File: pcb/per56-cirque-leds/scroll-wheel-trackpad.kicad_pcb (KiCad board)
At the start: 2 copper layers, 64.8 x 63.5 mm, 13 parts, among them J2 Conn_01x12_Female, SW1 RotaryEncoder

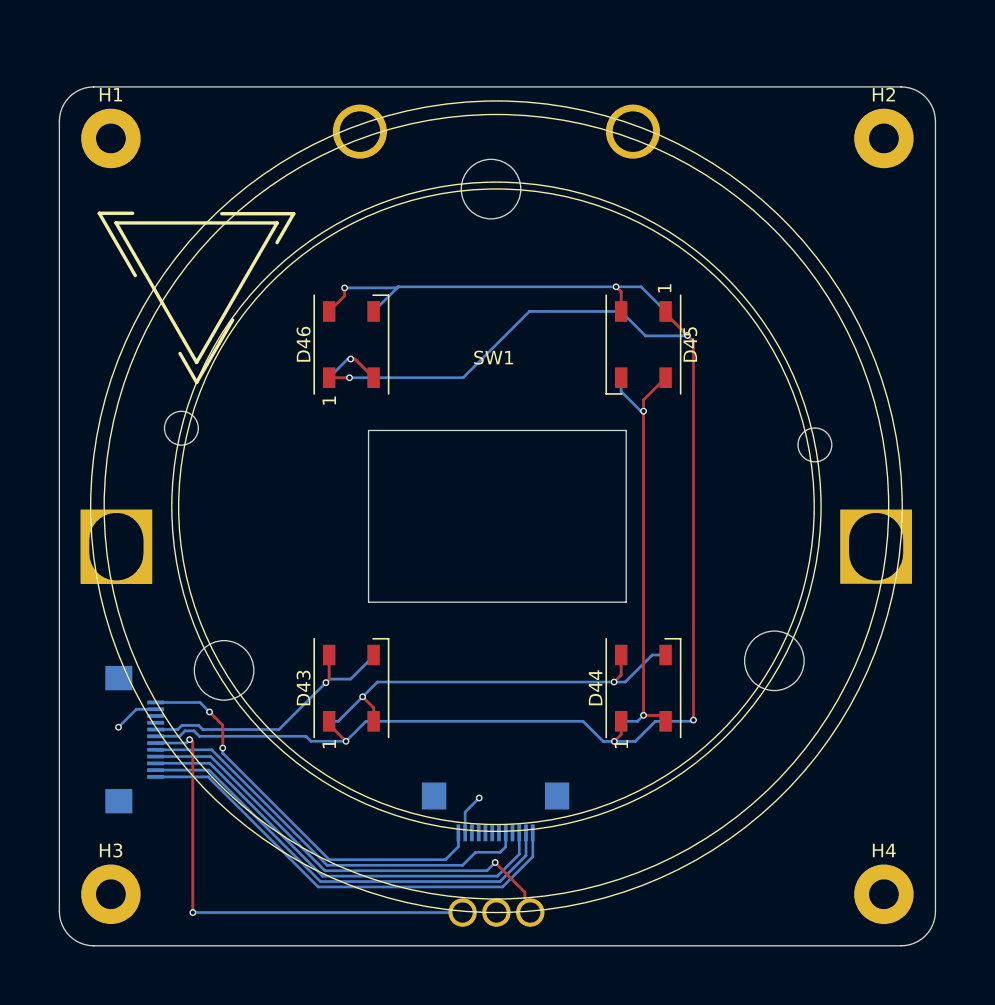
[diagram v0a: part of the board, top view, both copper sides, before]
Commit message: updated a few things, including standard pcb sizes and mounting, 3v3 logic level specification
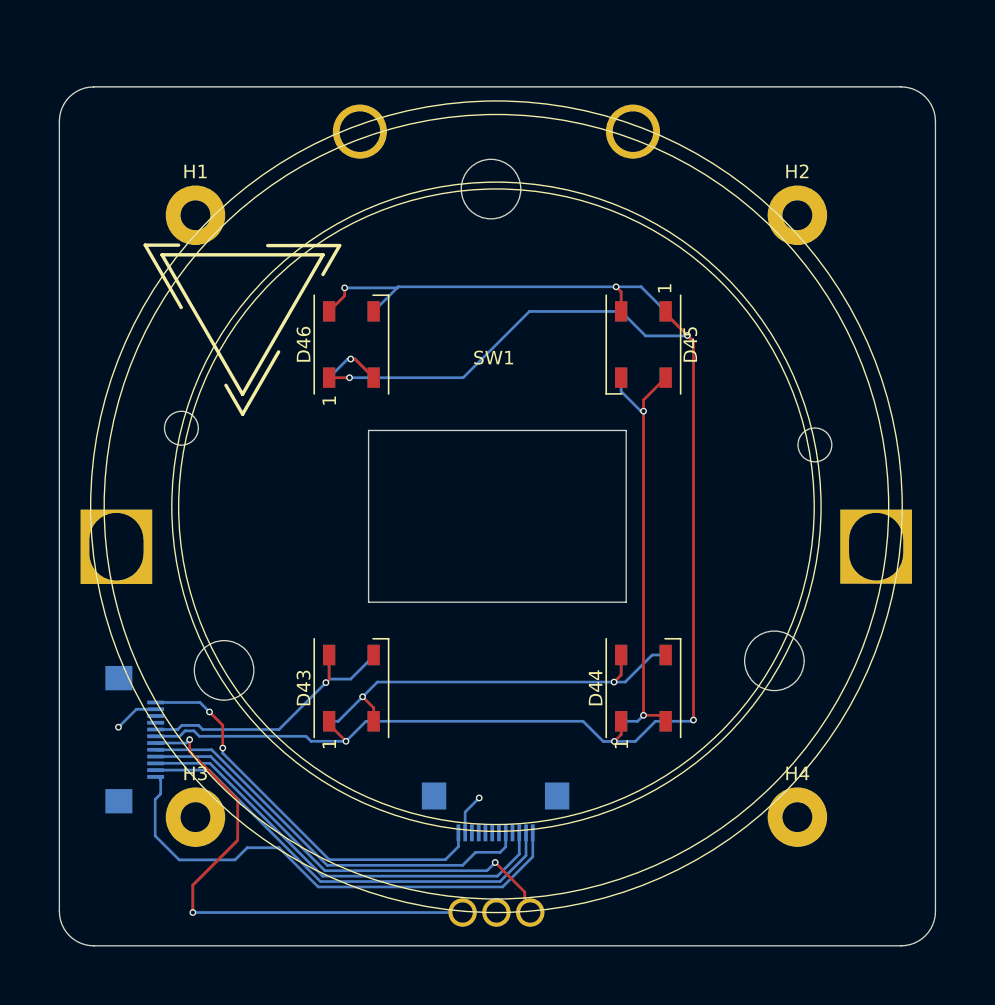
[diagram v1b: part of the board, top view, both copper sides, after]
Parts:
- moved H4 8.57 mm to (196.8, 142.9)
- moved H2 8.56 mm to (196.8, 98.4)
- moved H3 8.46 mm to (152.3, 142.9)
- moved H1 8.45 mm to (152.3, 98.4)
- moved REF** 4.13 mm to (155.8, 105.4) (x2)
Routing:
- net SCLK: track 33.9 -> 37.7 mm
- net GPIO_AD1: track 35.5 -> 38.2 mm
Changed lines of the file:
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@@
   )
   (footprint "MountingHole:MountingHole_2.2mm_M2_Pad" (layer "F.Cu")
-    (at 203.2 92.71)
+    (at 196.802257 98.39)
     (descr "Mounting Hole 2.2mm, M2")
     (tags "mounting hole 2.2mm m2")
@@
   )
   (footprint "MountingHole:MountingHole_2.2mm_M2_Pad" (layer "F.Cu")
-    (at 146.05 92.71)
+    (at 152.302257 98.39)
     (descr "Mounting Hole 2.2mm, M2")
     (tags "mounting hole 2.2mm m2")
@@
   )
   (footprint "MountingHole:MountingHole_2.2mm_M2_Pad" (layer "F.Cu")
-    (at 146.05 148.59)
+    (at 152.302257 142.89)
     (descr "Mounting Hole 2.2mm, M2")
     (tags "mounting hole 2.2mm m2")
@@
   )
   (footprint "MountingHole:MountingHole_2.2mm_M2_Pad" (layer "F.Cu")
-    (at 203.2 148.59)
+    (at 196.802257 142.89)
     (descr "Mounting Hole 2.2mm, M2")
     (tags "mounting hole 2.2mm m2")
@@
   )
   (footprint "fingerpunch:vik-logo-medium" (layer "F.Cu")
-    (at 152.375 103.025)
+    (at 155.771197 105.380578)
     (attr smd)
     (fp_text reference "REF**" (at -0.05 -6.96 unlocked) (layer "User.1")
@@
   )
   (footprint "fingerpunch:vik-logo-medium" (layer "B.Cu")
-    (at 152.375 103 180)
+    (at 155.771197 105.355578 180)
     (attr smd)
     (fp_text reference "REF**" (at -0.05 6.96 unlocked) (layer "User.1")
@@
   (segment (start 161.545686 147.65) (end 153.305686 139.41) (width 0.2) (layer "B.Cu") (net 18))
   (segment (start 174.82 147.65) (end 176.74 145.73) (width 0.2) (layer "B.Cu") (net 18))
+  (segment (start 149.358 139.91) (end 149.535 139.91) (width 0.2) (layer "B.Cu") (net 19))
   (segment (start 175.01 148.05) (end 177.24 145.82) (width 0.2) (layer "B.Cu") (net 19))
-  (segment (start 149.358 139.91) (end 153.24 139.91) (width 0.2) (layer "B.Cu") (net 19))
   (segment (start 161.38 148.05) (end 175.01 148.05) (width 0.2) (layer "B.Cu") (net 19))
-  (segment (start 153.24 139.91) (end 161.38 148.05) (width 0.2) (layer "B.Cu") (net 19))
+  (segment (start 151.1 146.05) (end 155.225 146.05) (width 0.2) (layer "B.Cu") (net 19))
+  (segment (start 149.535 139.91) (end 149.725 140.1) (width 0.2) (layer "B.Cu") (net 19))
+  (segment (start 158.48 145.15) (end 161.38 148.05) (width 0.2) (layer "B.Cu") (net 19))
+  (segment (start 156.125 145.15) (end 158.48 145.15) (width 0.2) (layer "B.Cu") (net 19))
+  (segment (start 149.725 141.175) (end 149.325 141.575) (width 0.2) (layer "B.Cu") (net 19))
+  (segment (start 149.725 140.1) (end 149.725 141.175) (width 0.2) (layer "B.Cu") (net 19))
   (segment (start 177.24 145.82) (end 177.24 144.048) (width 0.2) (layer "B.Cu") (net 19))
-  (segment (start 152.11 137.31) (end 151.96 137.16) (width 0.2) (layer "F.Cu") (net 21))
-  (segment (start 152.11 149.94) (end 152.11 137.31) (width 0.2) (layer "F.Cu") (net 21))
-  (segment (start 151.96 137.16) (end 151.87 137.16) (width 0.2) (layer "F.Cu") (net 21))
+  (segment (start 149.325 141.575) (end 149.325 144.275) (width 0.2) (layer "B.Cu") (net 19))
+  (segment (start 155.225 146.05) (end 156.125 145.15) (width 0.2) (layer "B.Cu") (net 19))
+  (segment (start 149.325 144.275) (end 151.1 146.05) (width 0.2) (layer "B.Cu") (net 19))
+  (segment (start 152.11 147.915) (end 155.425 144.6) (width 0.2) (layer "F.Cu") (net 21))
+  (segment (start 151.87 138.045) (end 151.87 137.16) (width 0.2) (layer "F.Cu") (net 21))
+  (segment (start 155.425 141.6) (end 151.87 138.045) (width 0.2) (layer "F.Cu") (net 21))
+  (segment (start 155.425 144.6) (end 155.425 141.6) (width 0.2) (layer "F.Cu") (net 21))
+  (segment (start 152.11 149.94) (end 152.11 147.915) (width 0.2) (layer "F.Cu") (net 21))
   (via (at 152.11 149.94) (size 0.5) (drill 0.3) (layers "F.Cu" "B.Cu") (net 21))
   (via (at 151.87 137.16) (size 0.5) (drill 0.3) (layers "F.Cu" "B.Cu") (net 21))

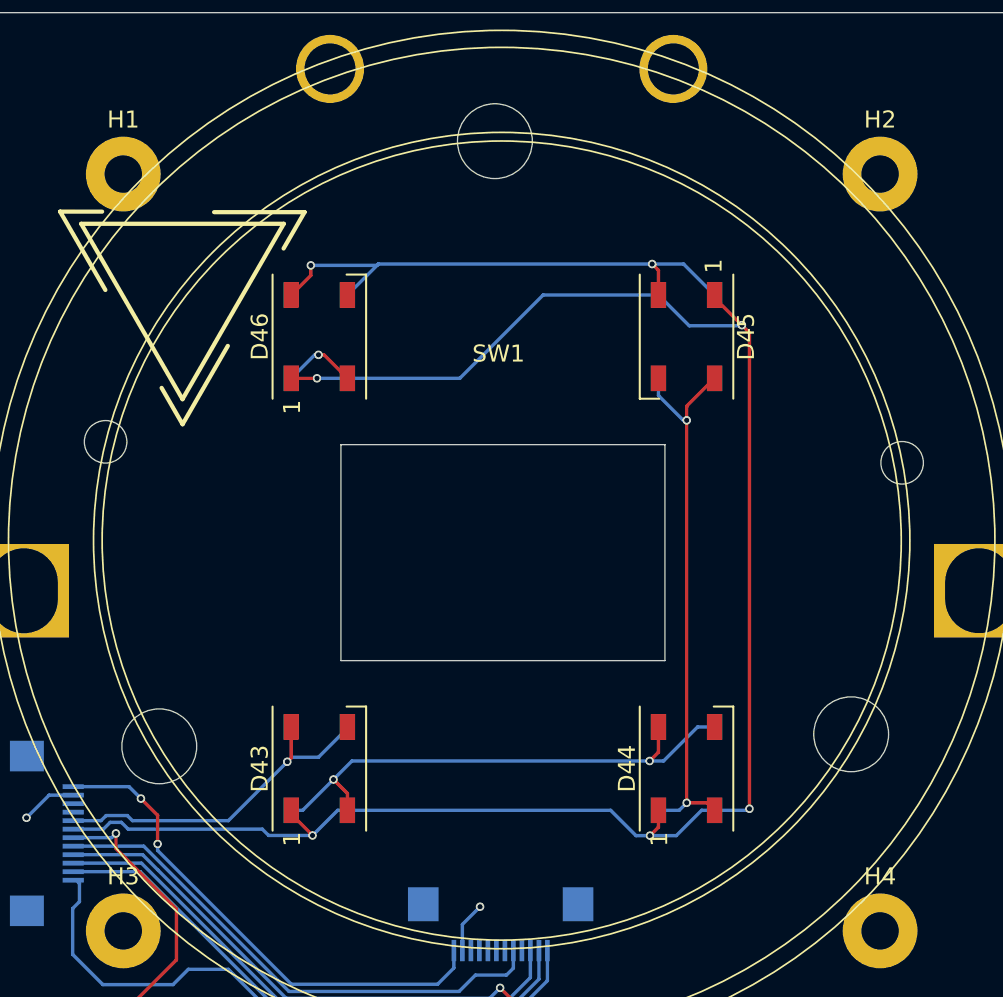
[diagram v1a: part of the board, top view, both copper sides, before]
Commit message: added module mounting footprints to make designing both the module pcbs and the keyboard pcbs mounting for modules easier
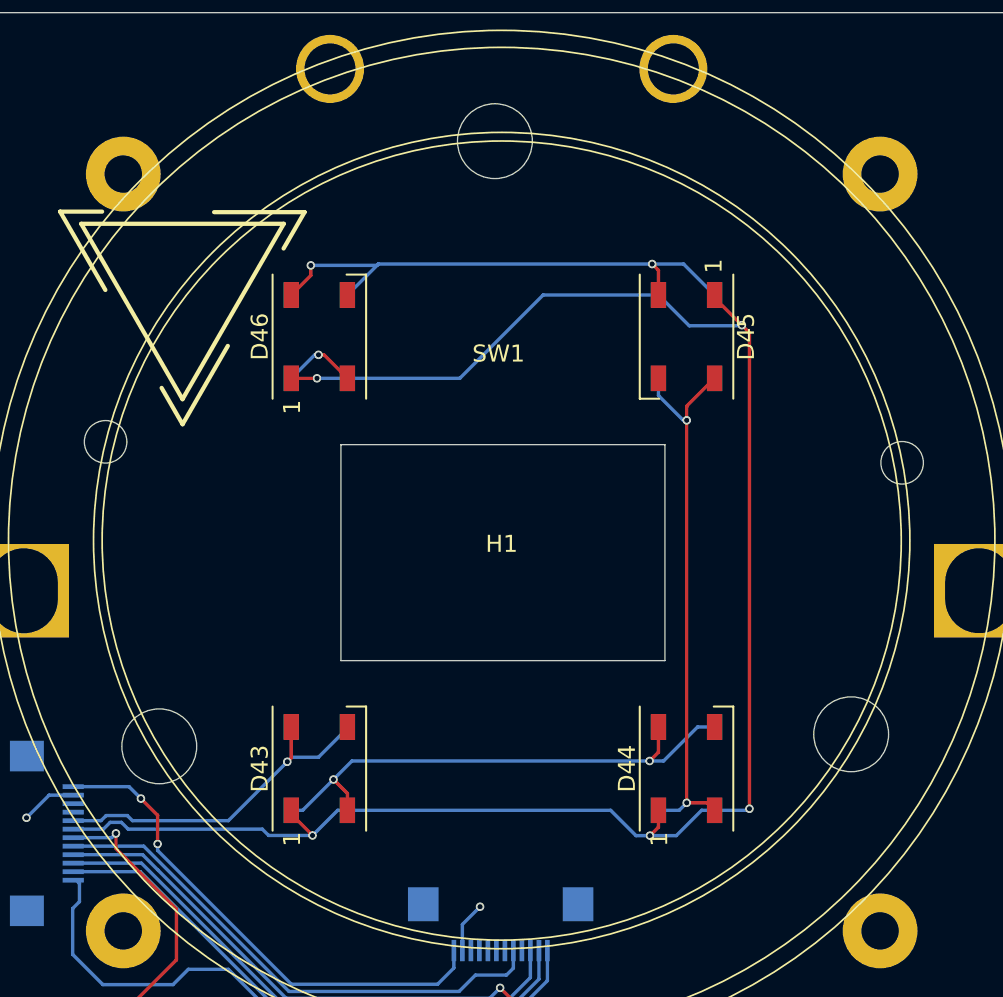
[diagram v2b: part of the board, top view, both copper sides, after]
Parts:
- removed H2, H3, H4: MountingHole, MountingHole:MountingHole_2.2mm_M2_Pad
- H1: footprint MountingHole:MountingHole_2.2mm_M2_Pad -> vik:vik-module-mounting-large
- moved H1 31.5 mm to (174.6, 120.6)
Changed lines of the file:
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@@
     )
   )
-  (footprint "MountingHole:MountingHole_2.2mm_M2_Pad" (layer "F.Cu")
-    (at 196.802257 98.39)
-    (descr "Mounting Hole 2.2mm, M2")
-    (tags "mounting hole 2.2mm m2")
+  (footprint "vik:vik-module-mounting-large" (layer "F.Cu")
+    (at 174.552 120.64)
     (property "Sheetfile" "scroll-wheel-trackpad.kicad_sch")
     (property "Sheetname" "")
     (property "ki_description" "Mounting Hole without connection")
     (property "ki_keywords" "mounting hole")
-    (attr exclude_from_pos_files)
-    (fp_text reference "H2" (at 0 -3.2) (layer "F.SilkS")
-        (effects (font (size 1 1) (thickness 0.15)))
-    )
-    (fp_text value "MountingHole" (at 0 3.2) (layer "F.Fab")
-        (effects (font (size 1 1) (thickness 0.15)))
-    )
-    (fp_text user "${REFERENCE}" (at 0 0) (layer "F.Fab")
-        (effects (font (size 1 1) (thickness 0.15)))
-    )
-    (fp_circle (center 0 0) (end 2.2 0)
+    (attr through_hole)
+    (fp_text reference "H1" (at 0 -0.5 unlocked) (layer "F.SilkS")
+        (effects (font (size 1 1) (thickness 0.15)))
+    )
+    (fp_text value "MountingHole" (at 0 1 unlocked) (layer "F.Fab")
+        (effects (font (size 1 1) (thickness 0.15)))
+    )
+    (fp_text user "${REFERENCE}" (at 22.250257 -22.25) (layer "F.Fab")
+        (effects (font (size 1 1) (thickness 0.15)))
+    )
+    (fp_text user "${REFERENCE}" (at -22.249743 22.25) (layer "F.Fab")
+        (effects (font (size 1 1) (thickness 0.15)))
+    )
+    (fp_text user "${REFERENCE}" (at -22.249743 -22.25) (layer "F.Fab")
+        (effects (font (size 1 1) (thickness 0.15)))
+    )
+    (fp_text user "${REFERENCE}" (at 22.250257 22.25) (layer "F.Fab")
+        (effects (font (size 1 1) (thickness 0.15)))
+    )
+    (fp_text user "${REFERENCE}" (at 0 2.5 unlocked) (layer "F.Fab")
+        (effects (font (size 1 1) (thickness 0.15)))
+    )
+    (fp_line (start -32.5 -29.766797) (end -32.5 29.768411)
+      (stroke (width 0.05) (type solid)) (layer "Dwgs.User"))
+    (fp_line (start -29.77 32.5) (end 29.782 32.5)
+      (stroke (width 0.05) (type solid)) (layer "Dwgs.User"))
+    (fp_line (start 29.779935 -32.5) (end -29.772 -32.5)
+      (stroke (width 0.05) (type solid)) (layer "Dwgs.User"))
+    (fp_line (start 32.5 29.76) (end 32.5 -29.768411)
+      (stroke (width 0.05) (type solid)) (layer "Dwgs.User"))
+    (fp_arc (start -32.5 -29.766797) (mid -31.702064 -31.698385) (end -29.772 -32.5)
+      (stroke (width 0.05) (type solid)) (layer "Dwgs.User"))
+    (fp_arc (start -29.772 32.5) (mid -31.701731 31.699193) (end -32.5 29.768411)
+      (stroke (width 0.05) (type solid)) (layer "Dwgs.User"))
+    (fp_arc (start 29.779935 -32.5) (mid 31.705706 -31.697557) (end 32.5 -29.768411)
+      (stroke (width 0.05) (type solid)) (layer "Dwgs.User"))
+    (fp_arc (start 32.5 29.76) (mid 31.708473 31.692916) (end 29.782 32.5)
+      (stroke (width 0.05) (type solid)) (layer "Dwgs.User"))
+    (fp_circle (center -22.249743 -22.25) (end -20.049743 -22.25)
       (stroke (width 0.15) (type solid)) (fill none) (layer "Cmts.User"))
-    (fp_circle (center 0 0) (end 2.45 0)
+    (fp_circle (center -22.249743 22.25) (end -20.049743 22.25)
+      (stroke (width 0.15) (type solid)) (fill none) (layer "Cmts.User"))
+    (fp_circle (center 22.250257 -22.25) (end 24.450257 -22.25)
+      (stroke (width 0.15) (type solid)) (fill none) (layer "Cmts.User"))
+    (fp_circle (center 22.250257 22.25) (end 24.450257 22.25)
+      (stroke (width 0.15) (type solid)) (fill none) (layer "Cmts.User"))
+    (fp_circle (center -22.249743 -22.25) (end -19.799743 -22.25)
       (stroke (width 0.05) (type solid)) (fill none) (layer "F.CrtYd"))
-    (pad "1" thru_hole circle (at 0 0) (size 4.4 4.4) (drill 2.2) (layers "*.Cu" "*.Mask"))
-  )
-  (footprint "MountingHole:MountingHole_2.2mm_M2_Pad" (layer "F.Cu")
-    (at 152.302257 98.39)
-    (descr "Mounting Hole 2.2mm, M2")
-    (tags "mounting hole 2.2mm m2")
-    (property "Sheetfile" "scroll-wheel-trackpad.kicad_sch")
-    (property "Sheetname" "")
-    (property "ki_description" "Mounting Hole without connection")
-    (property "ki_keywords" "mounting hole")
-    (attr exclude_from_pos_files)
-    (fp_text reference "H1" (at 0 -3.2) (layer "F.SilkS")
-        (effects (font (size 1 1) (thickness 0.15)))
-    )
-    (fp_text value "MountingHole" (at 0 3.2) (layer "F.Fab")
-        (effects (font (size 1 1) (thickness 0.15)))
-    )
-    (fp_text user "${REFERENCE}" (at 0 0) (layer "F.Fab")
-        (effects (font (size 1 1) (thickness 0.15)))
-    )
-    (fp_circle (center 0 0) (end 2.2 0)
-      (stroke (width 0.15) (type solid)) (fill none) (layer "Cmts.User"))
-    (fp_circle (center 0 0) (end 2.45 0)
+    (fp_circle (center -22.249743 22.25) (end -19.799743 22.25)
       (stroke (width 0.05) (type solid)) (fill none) (layer "F.CrtYd"))
-    (pad "1" thru_hole circle (at 0 0) (size 4.4 4.4) (drill 2.2) (layers "*.Cu" "*.Mask"))
+    (fp_circle (center 22.250257 -22.25) (end 24.700257 -22.25)
+      (stroke (width 0.05) (type solid)) (fill none) (layer "F.CrtYd"))
+    (fp_circle (center 22.250257 22.25) (end 24.700257 22.25)
+      (stroke (width 0.05) (type solid)) (fill none) (layer "F.CrtYd"))
+    (pad "1" thru_hole circle (at -22.249743 -22.25) (size 4.4 4.4) (drill 2.2) (layers "*.Cu" "*.Mask"))
+    (pad "1" thru_hole circle (at -22.249743 22.25) (size 4.4 4.4) (drill 2.2) (layers "*.Cu" "*.Mask"))
+    (pad "1" thru_hole circle (at 22.250257 -22.25) (size 4.4 4.4) (drill 2.2) (layers "*.Cu" "*.Mask"))
+    (pad "1" thru_hole circle (at 22.250257 22.25) (size 4.4 4.4) (drill 2.2) (layers "*.Cu" "*.Mask"))
   )
   (footprint "fingerpunch:LED_WS2812B_PLCC4_5.0x5.0mm_P3.2mm-reversible" (layer "F.Cu")
@@
     )
   )
-  (footprint "MountingHole:MountingHole_2.2mm_M2_Pad" (layer "F.Cu")
-    (at 152.302257 142.89)
-    (descr "Mounting Hole 2.2mm, M2")
-    (tags "mounting hole 2.2mm m2")
-    (property "Sheetfile" "scroll-wheel-trackpad.kicad_sch")
-    (property "Sheetname" "")
-    (property "ki_description" "Mounting Hole without connection")
-    (property "ki_keywords" "mounting hole")
-    (attr exclude_from_pos_files)
-    (fp_text reference "H3" (at 0 -3.2) (layer "F.SilkS")
-        (effects (font (size 1 1) (thickness 0.15)))
-    )
-    (fp_text value "MountingHole" (at 0 3.2) (layer "F.Fab")
-        (effects (font (size 1 1) (thickness 0.15)))
-    )
-    (fp_text user "${REFERENCE}" (at 0 0) (layer "F.Fab")
-        (effects (font (size 1 1) (thickness 0.15)))
-    )
-    (fp_circle (center 0 0) (end 2.2 0)
-      (stroke (width 0.15) (type solid)) (fill none) (layer "Cmts.User"))
-    (fp_circle (center 0 0) (end 2.45 0)
-      (stroke (width 0.05) (type solid)) (fill none) (layer "F.CrtYd"))
-    (pad "1" thru_hole circle (at 0 0) (size 4.4 4.4) (drill 2.2) (layers "*.Cu" "*.Mask"))
-  )
-  (footprint "MountingHole:MountingHole_2.2mm_M2_Pad" (layer "F.Cu")
-    (at 196.802257 142.89)
-    (descr "Mounting Hole 2.2mm, M2")
-    (tags "mounting hole 2.2mm m2")
-    (property "Sheetfile" "scroll-wheel-trackpad.kicad_sch")
-    (property "Sheetname" "")
-    (property "ki_description" "Mounting Hole without connection")
-    (property "ki_keywords" "mounting hole")
-    (attr exclude_from_pos_files)
-    (fp_text reference "H4" (at 0 -3.2) (layer "F.SilkS")
-        (effects (font (size 1 1) (thickness 0.15)))
-    )
-    (fp_text value "MountingHole" (at 0 3.2) (layer "F.Fab")
-        (effects (font (size 1 1) (thickness 0.15)))
-    )
-    (fp_text user "${REFERENCE}" (at 0 0) (layer "F.Fab")
-        (effects (font (size 1 1) (thickness 0.15)))
-    )
-    (fp_circle (center 0 0) (end 2.2 0)
-      (stroke (width 0.15) (type solid)) (fill none) (layer "Cmts.User"))
-    (fp_circle (center 0 0) (end 2.45 0)
-      (stroke (width 0.05) (type solid)) (fill none) (layer "F.CrtYd"))
-    (pad "1" thru_hole circle (at 0 0) (size 4.4 4.4) (drill 2.2) (layers "*.Cu" "*.Mask"))
-  )
   (footprint "fingerpunch:LED_WS2812B_PLCC4_5.0x5.0mm_P3.2mm-reversible" (layer "F.Cu")
